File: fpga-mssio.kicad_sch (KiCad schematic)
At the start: 14 parts, among them U1 MPFS250T-FCVG484, U30 NTS0102_XSON

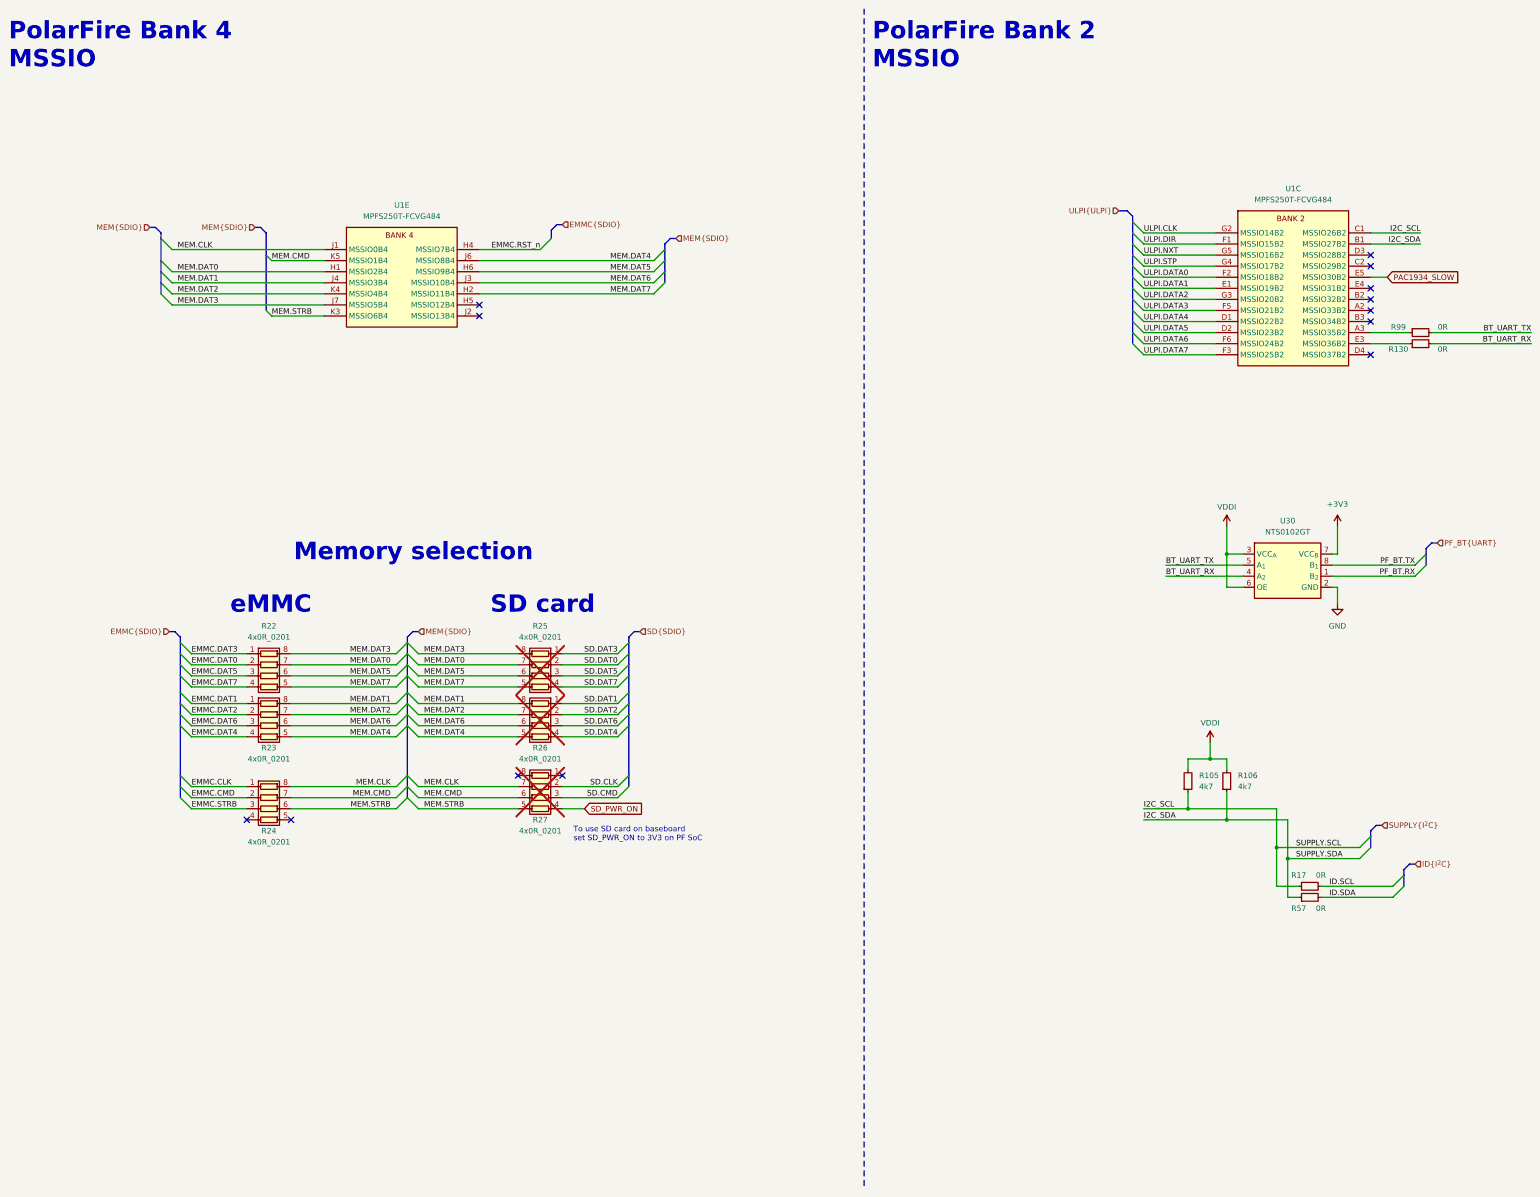
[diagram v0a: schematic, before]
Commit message: [#59910] Align buses, updated symbols and clean ERC
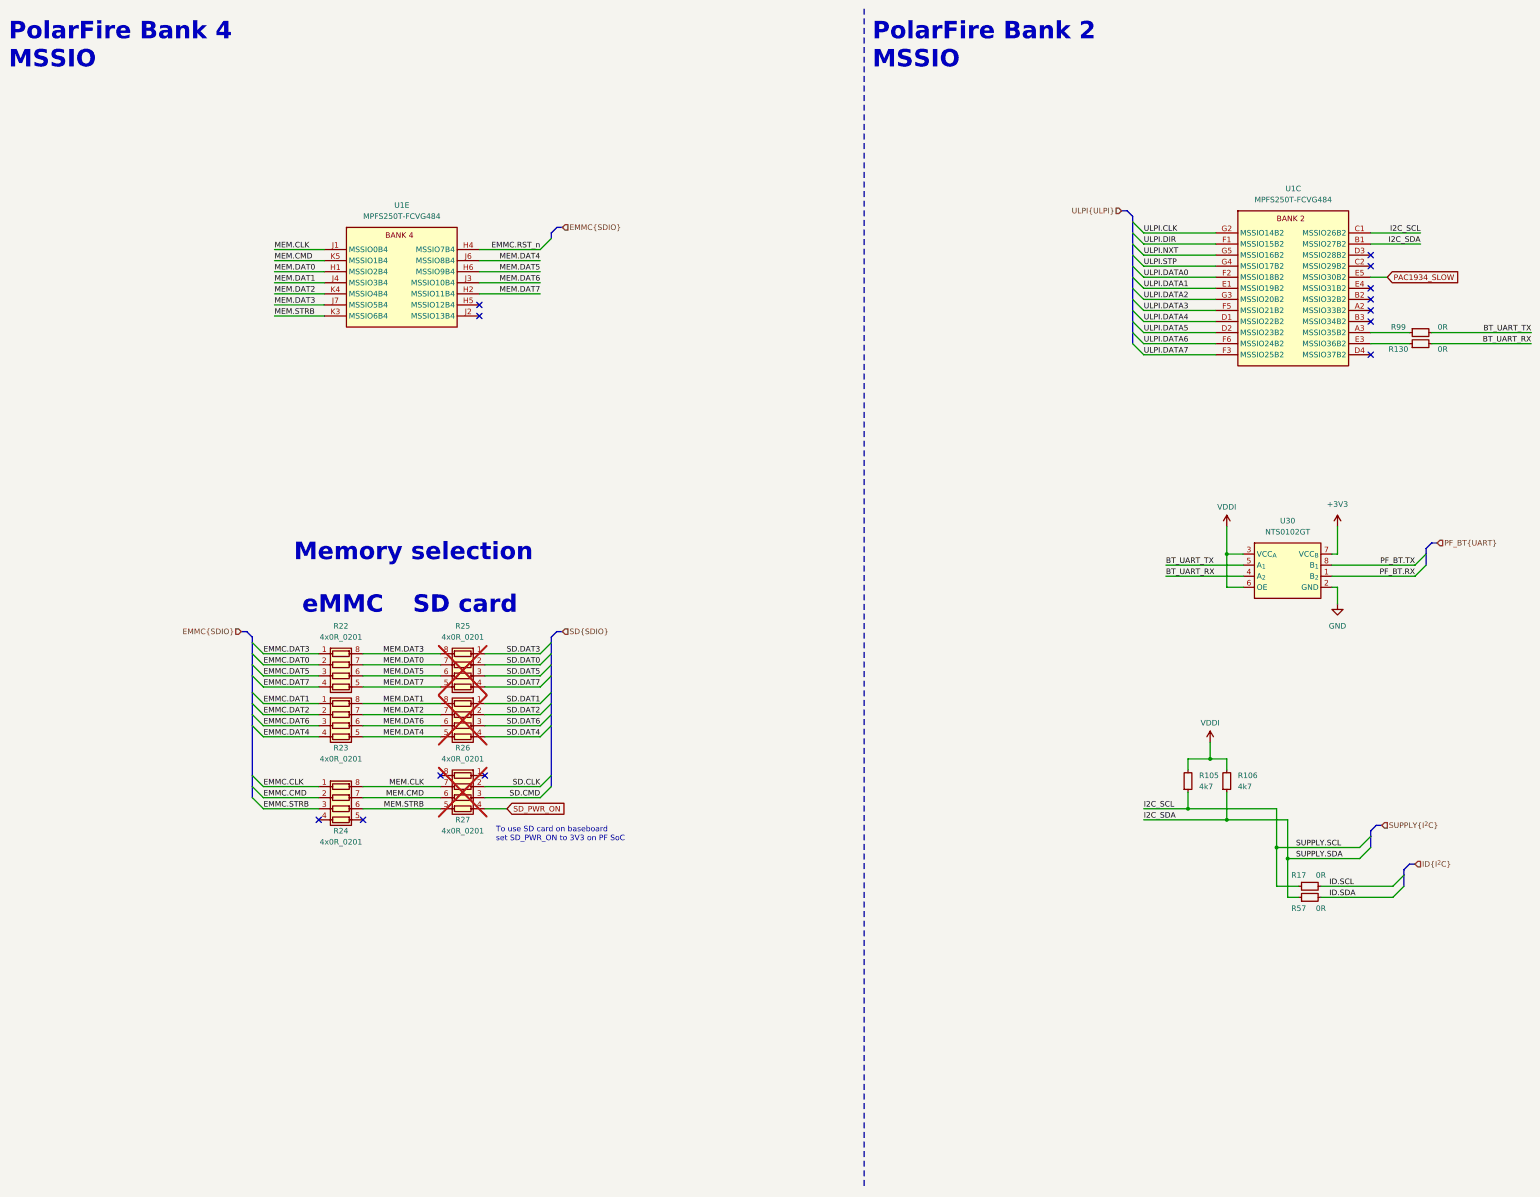
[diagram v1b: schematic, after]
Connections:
- net VDDI renamed VDD
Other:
- moved on the sheet: R22, R23, R24, R25, R26, R27

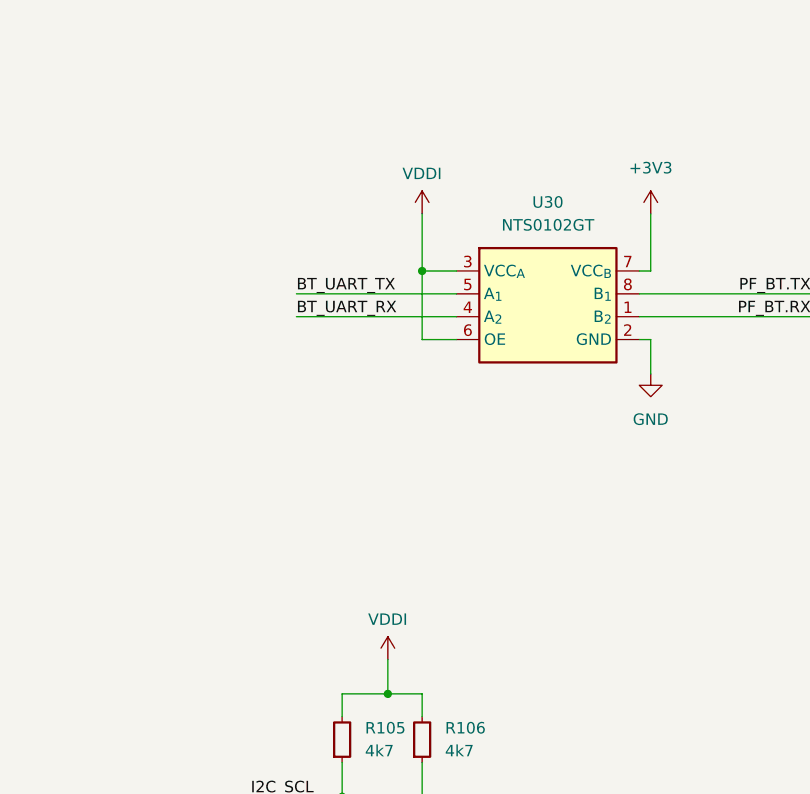
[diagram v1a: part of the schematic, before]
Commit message: [#73079] Migrate project to KiCad 8. Clean DRCs
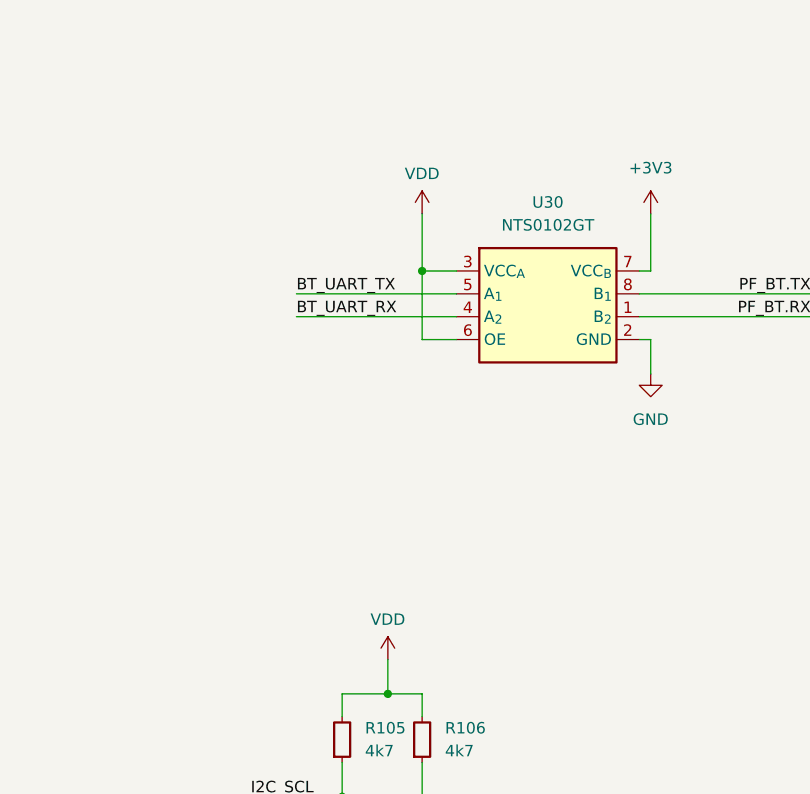
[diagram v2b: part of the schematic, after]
